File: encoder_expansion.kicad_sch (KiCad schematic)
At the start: 7 parts, among them J1 Conn_01x05_Socket, J2 Conn_01x05_Socket, J3 Conn_01x04_Socket, J4 Conn_01x04_Socket, J5 Conn_01x04_Socket, J6 Conn_01x04_Socket, J7 Conn_01x02_Socket

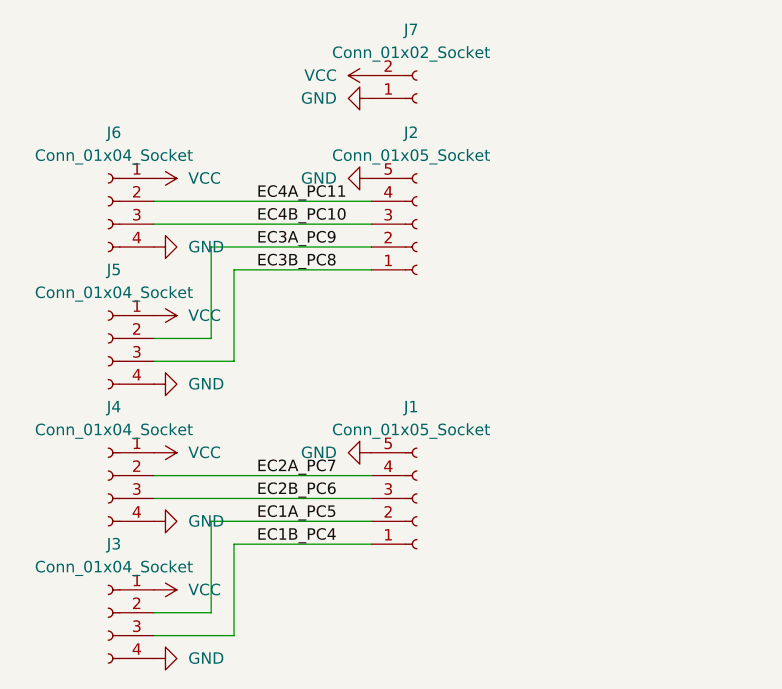
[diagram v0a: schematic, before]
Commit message: add mounting hole and silk
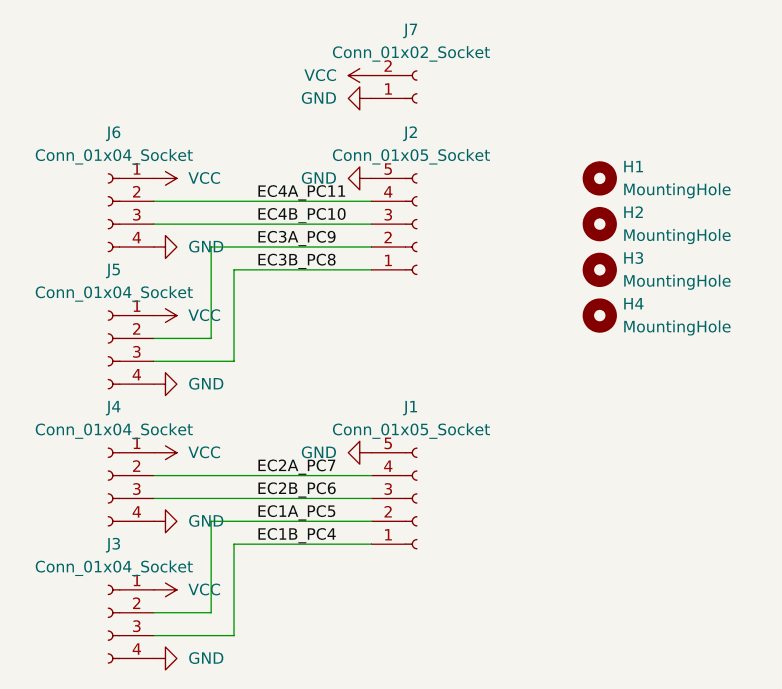
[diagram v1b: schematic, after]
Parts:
- added H1, H2, H3, H4: MountingHole, MountingHole:MountingHole_3.2mm_M3_Pad_Via, symbol Mechanical:MountingHole
